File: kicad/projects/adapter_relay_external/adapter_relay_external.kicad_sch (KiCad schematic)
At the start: 12 parts, among them J1 M5Stack A117 PinHeader, J2 M5Stack A117 PinSocket, J3 DC-0440-2.5A-2.0, U1 Optocoupler

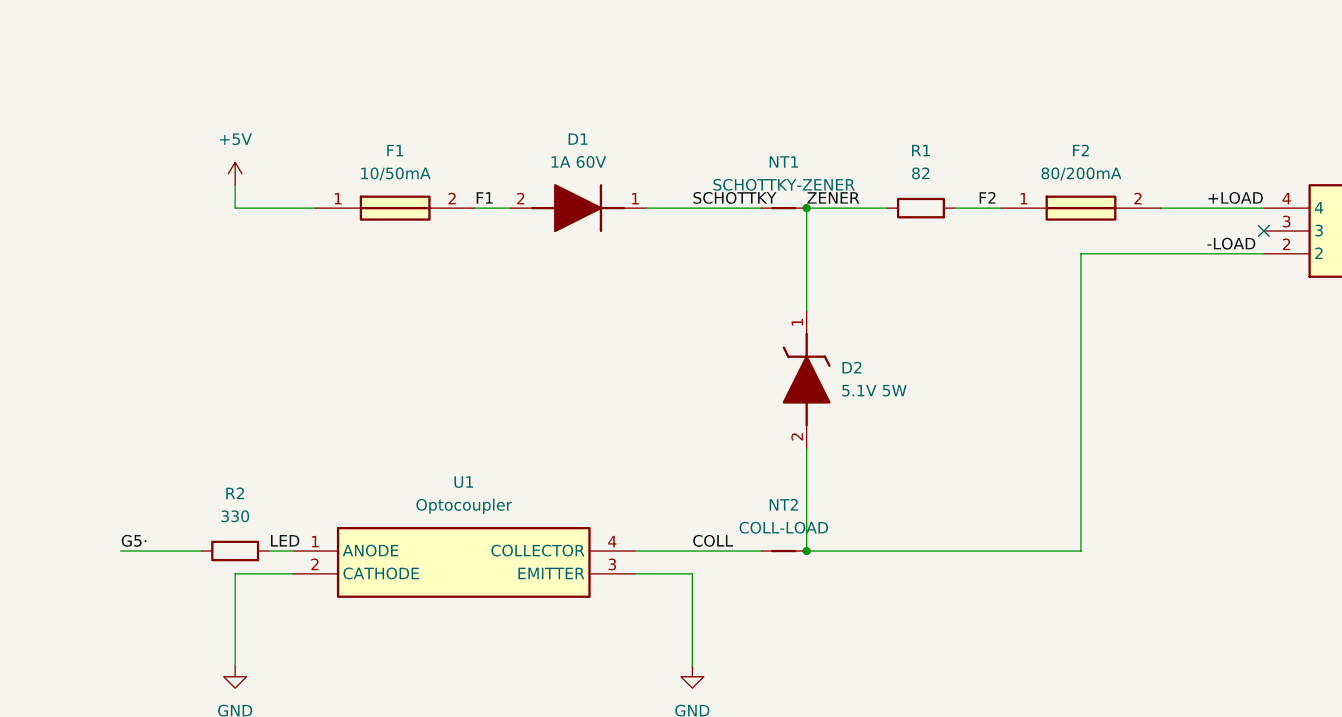
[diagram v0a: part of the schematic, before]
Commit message: move dc jack, tune R1 spec, add gpio pin
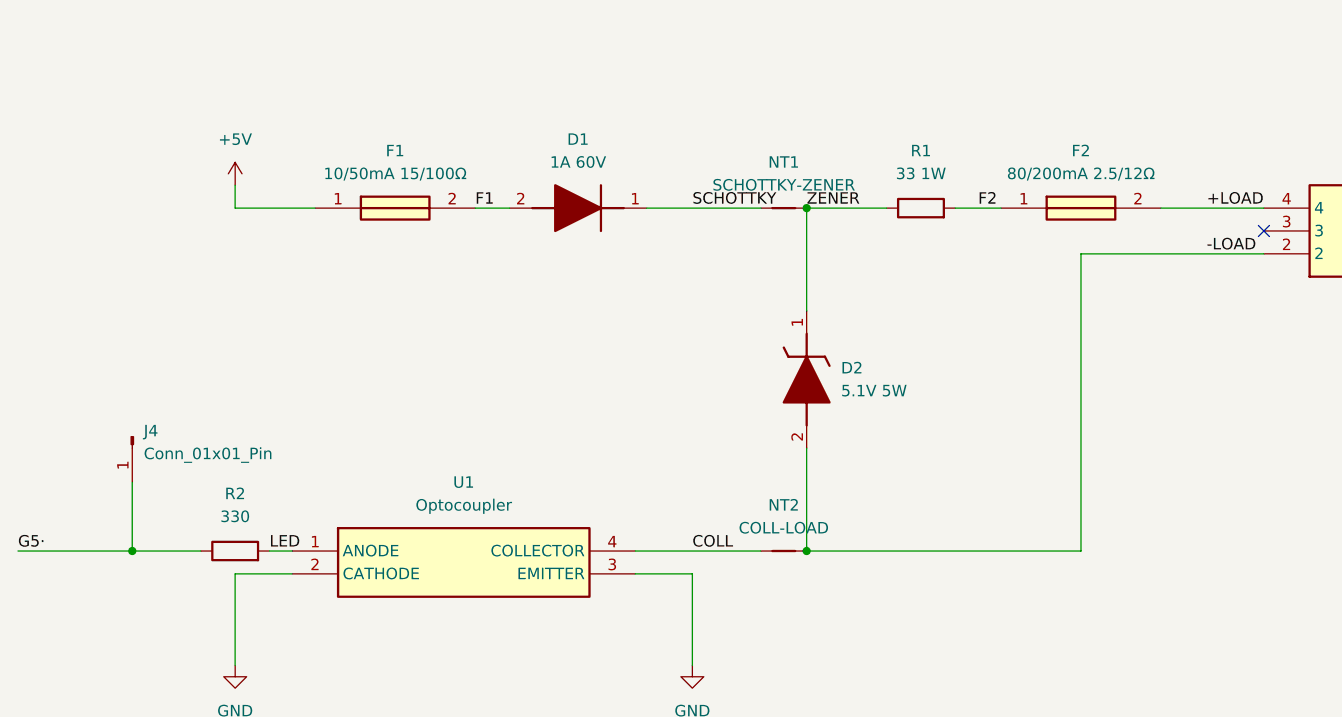
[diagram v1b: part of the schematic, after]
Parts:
- added J4: Conn_01x01_Pin, Connector_PinHeader_1.00mm:PinHeader_1x01_P1.00mm_Vertical, symbol Connector:Conn_01x01_Pin
- F1: value 10/50mA -> 10/50mA 15/100Ω
- F2: value 80/200mA -> 80/200mA 2.5/12Ω
- R1: value 82 -> 33 1W; Mouser Part Number 667-ERJ-P14F82R0U -> 755-ESR25JZPJ330; Vendor https://www.mouser.com/ProductDetail/Panasonic/ERJ-P14F82R0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 -> https://www.mouser.com/ProductDetail/ROHM-Semiconductor/ESR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
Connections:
- net G5·: now also J4.1 (Pin_1)
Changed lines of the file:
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@@
+	)
+	(junction
+		(at 46.99 165.1)
+		(diameter 0)
+		(color 0 0 0 0)
 	)
 	(junction
@@
 	(wire
 		(pts
-			(xy 45.72 165.1) (xy 54.61 165.1)
+			(xy 46.99 157.48) (xy 46.99 165.1)
+		)
+		(stroke
+			(width 0)
+			(type default)
+		)
+	)
+	(wire
+		(pts
+			(xy 34.29 165.1) (xy 46.99 165.1)
 		)
 		(stroke
@@
 		(pts
 			(xy 104.14 127) (xy 116.84 127)
+		)
+		(stroke
+			(width 0)
+			(type default)
+		)
+	)
+	(wire
+		(pts
+			(xy 46.99 165.1) (xy 54.61 165.1)
 		)
 		(stroke
@@
 	)
 	(label "G5·"
-		(at 45.72 165.1 0)
+		(at 34.29 165.1 0)
 		(effects
 			(font
@@
 			)
 		)
-		(property "Value" "82"
+		(property "Value" "33 1W"
 			(at 134.62 123.19 90)
 			(effects
@@
 			)
 		)
-		(property "Datasheet" "https://industrial.panasonic.com/cdbs/www-data/pdf/RDO0000/AOA0000C331.pdf"
+		(property "Datasheet" "https://fscdn.rohm.com/en/products/databook/datasheet/passive/resistor/chip_resistor/esr-e.pdf"
 			(at 134.62 127 0)
 			(effects
@@
 			)
 		)
-		(property "Mouser Part Number" "667-ERJ-P14F82R0U"
+		(property "Mouser Part Number" "755-ESR25JZPJ330 "
 			(at 134.62 127 90)
 			(effects
@@
 			)
 		)
-		(property "Vendor" "https://www.mouser.com/ProductDetail/Panasonic/ERJ-P14F82R0U?qs=sGAEpiMZZMtG0KNrPCHnjXA8RZptup0%2FUObEYYeTHU4%3D"
+		(property "Vendor" "https://www.mouser.com/ProductDetail/ROHM-Semiconductor/ESR25JZPJ330?qs=493kPxzlxfJQrSS8wBFbnw%3D%3D"
 			(at 134.62 127 90)
 			(effects
@@
 			)
 		)
-		(property "Value" "10/50mA"
+		(property "Value" "10/50mA 15/100Ω"
 			(at 76.2 123.19 0)
 			(effects
@@
 			)
 		)
-		(property "Value" "80/200mA"
+		(property "Value" "80/200mA 2.5/12Ω"
 			(at 152.4 123.19 0)
 			(effects
@@
 					(unit 1)
 				)
+			)
+		)
+	)
+	(symbol
+		(lib_id "Connector:Conn_01x01_Pin")
+		(at 46.99 152.4 270)
+		(unit 1)
+		(exclude_from_sim no)
+		(in_bom yes)
+		(on_board yes)
+		(dnp no)
+		(property "Reference" "J4"
+			(at 48.26 151.7649 90)
+			(effects
+				(font
+					(size 1.27 1.27)
+				)
+				(justify left)
+			)
+		)
+		(property "Value" "Conn_01x01_Pin"
+			(at 48.26 154.3049 90)
+			(effects
+				(font
+					(size 1.27 1.27)
+				)
+				(justify left)
+			)
+		)
+		(property "Footprint" "Connector_PinHeader_1.00mm:PinHeader_1x01_P1.00mm_Vertical"
+			(at 46.99 152.4 0)
+			(effects
+				(font
+					(size 1.27 1.27)
+				)
+				(hide yes)
+			)
+		)
+		(property "Datasheet" "~"
+			(at 46.99 152.4 0)
+			(effects
+				(font
+					(size 1.27 1.27)
+				)
+				(hide yes)
+			)
+		)
+		(property "Description" "Generic connector, single row, 01x01, script generated"
+			(at 46.99 152.4 0)
+			(effects
+				(font
+					(size 1.27 1.27)
+				)
+				(hide yes)
+			)
+		)
+		(pin "1"
+		)
+		(instances
+			(project ""
+				(path "/c325f515-49a7-4120-a4a4-460f32936e5c"
+					(reference "J4")
+					(unit 1)
+				)
